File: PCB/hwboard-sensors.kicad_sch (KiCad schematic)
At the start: 0 parts

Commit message: add sensors
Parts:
- added U6: LPS22DF, Package_LGA:ST_HLGA-10_2x2mm_P0.5mm_LayoutBorder3x2y, symbol Sensor_Pressure:LPS22DF
- added U7: LSM6DSM, Package_LGA:LGA-14_3x2.5mm_P0.5mm_LayoutBorder3x4y, symbol Sensor_Motion:LSM6DSM
- added U8: LIS2MDL, Package_LGA:LGA-12_2x2mm_P0.5mm, symbol Sensor_Magnetic:LIS2MDL
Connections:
- new net: U8.6 (GND), U8.8 (GND)
- new net: U7.6 (GND), U7.7 (GND)
- new net: U6.3 (GND), U6.9 (GND)
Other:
- note added: "LSM6DSVTR"

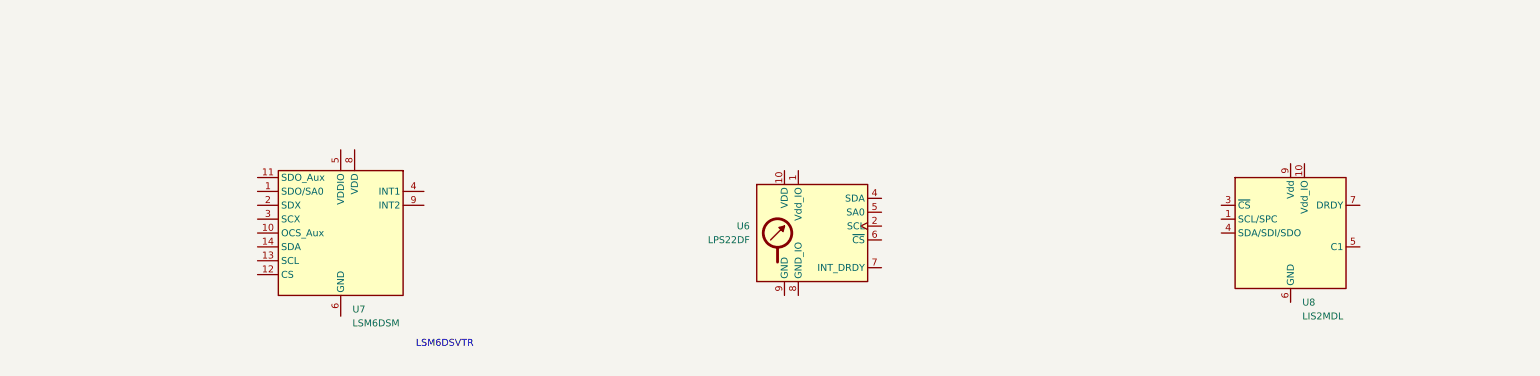
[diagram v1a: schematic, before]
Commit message: add sensors components
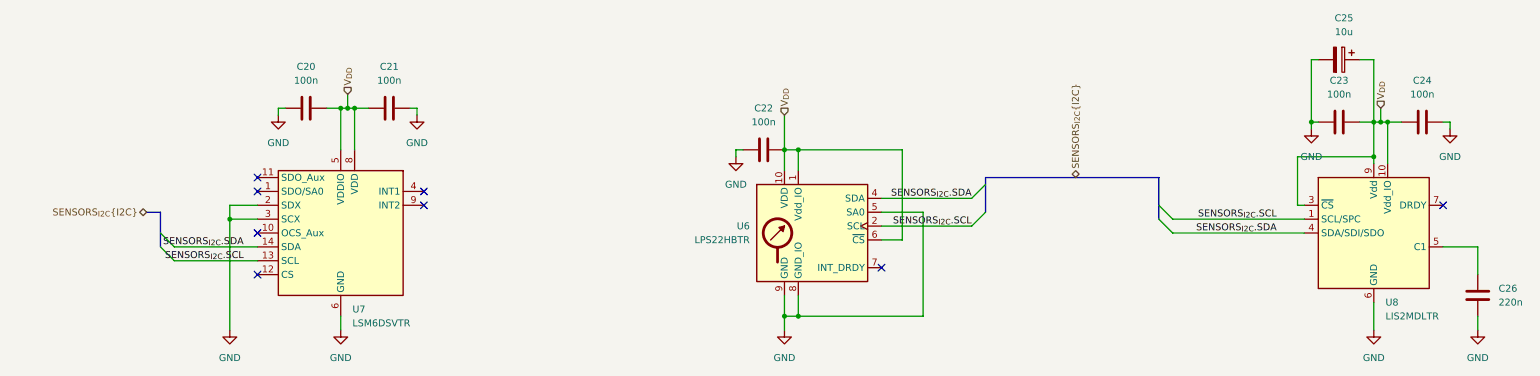
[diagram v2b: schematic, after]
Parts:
- added C20, C21, C22, C23, C24: 100n, symbol Device:C
- added C25: 10u, symbol Device:C_Polarized
- added C26: 220n, symbol Device:C
- U6: value LPS22DF -> LPS22HBTR; Manufacturer_Name (none) -> STMicroelectronics; Manufacturer_Part_Number (none) -> LPS22HBTR
- U7: value LSM6DSM -> LSM6DSVTR; Manufacturer_Name (none) -> STMicroelectronics; Manufacturer_Part_Number (none) -> LSM6DSVTR
- U8: value LIS2MDL -> LIS2MDLTR; Manufacturer_Name (none) -> STMicroelectronics; Manufacturer_Part_Number (none) -> LIS2MDLTR
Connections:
- net SENSORS_{I2C}.SCL: now reaches U8.1 (SCL/SPC)
- net SENSORS_{I2C}.SCL: now also U6.2 (SCL), U7.13 (SCL)
- net V_{DD}: now reaches U8.10 (Vdd_IO)
- net V_{DD}: now also U6.1 (Vdd_IO), U6.10 (VDD), U6.6 (~{CS}), U7.5 (VDDIO), U7.8 (VDD), U8.3 (~{CS}), U8.9 (Vdd), C20.2, C21.1, C22.2, C23.2, C24.1, C25.1
- net SENSORS_{I2C}.SDA: now reaches U8.4 (SDA/SDI/SDO)
- net SENSORS_{I2C}.SDA: now also U6.4 (SDA), U7.14 (SDA)
- net at U8.5 (C1): now also C26.2
- net GND: now reaches U8.6 (GND), U8.8 (GND)
- net GND: now also U6.3 (GND), U6.5 (SA0), U6.8 (GND_IO), U6.9 (GND), U7.2 (SDX), U7.3 (SCX), U7.6 (GND), U7.7 (GND), C20.1, C21.2, C22.1, C23.1, C24.2, C25.2, C26.1
- no-connect marks 0 -> 8
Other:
- note removed: "LSM6DSVTR"
- moved on the sheet: U8

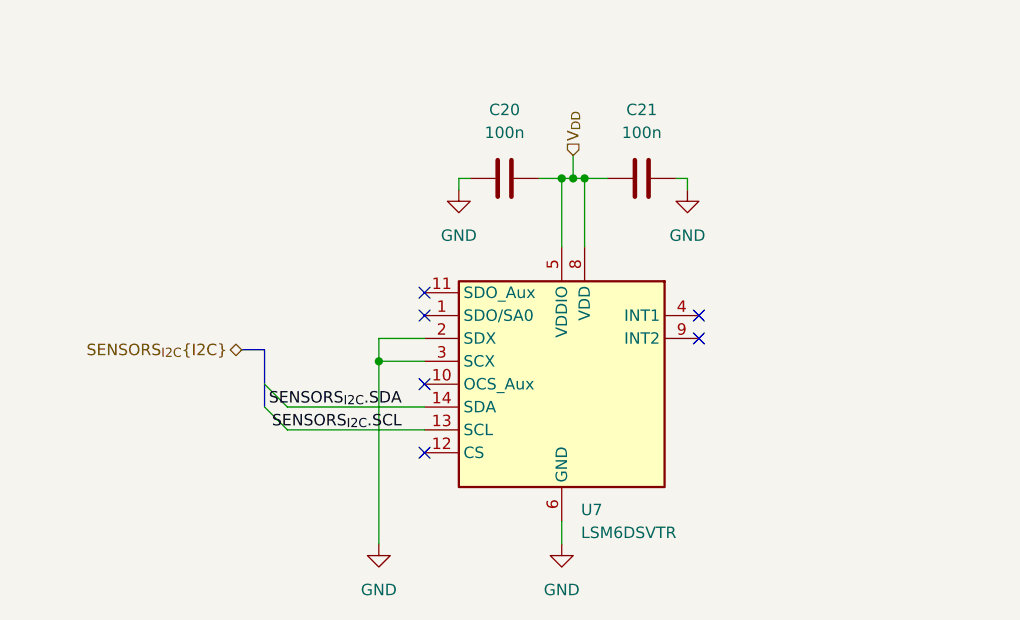
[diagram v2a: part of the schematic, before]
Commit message: add resistive touch IC
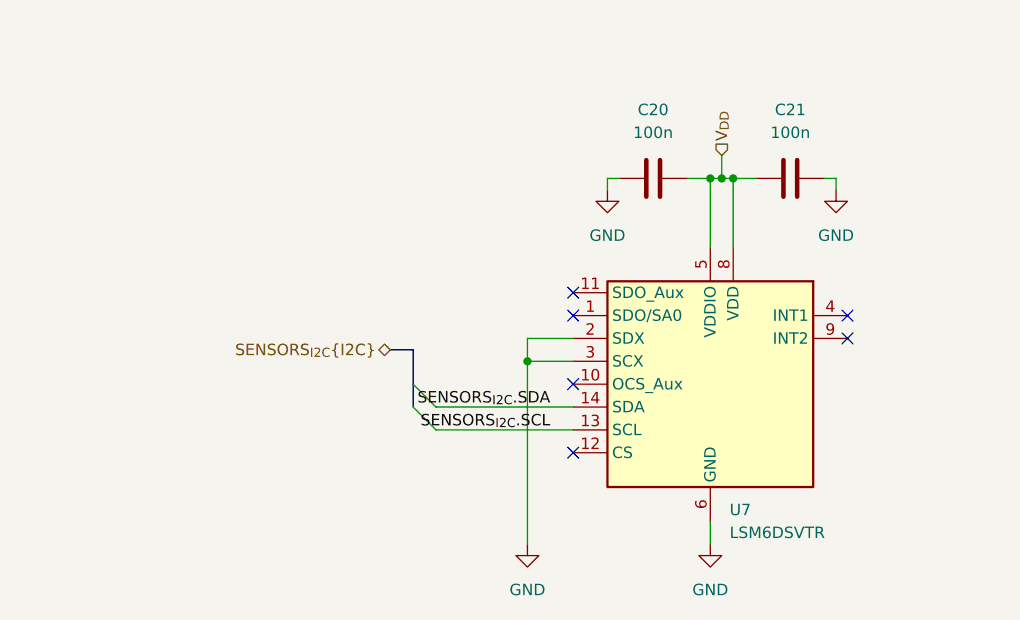
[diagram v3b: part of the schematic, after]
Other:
- moved on the sheet: C20, C21, U7
